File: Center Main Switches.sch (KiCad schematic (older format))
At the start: 120 parts

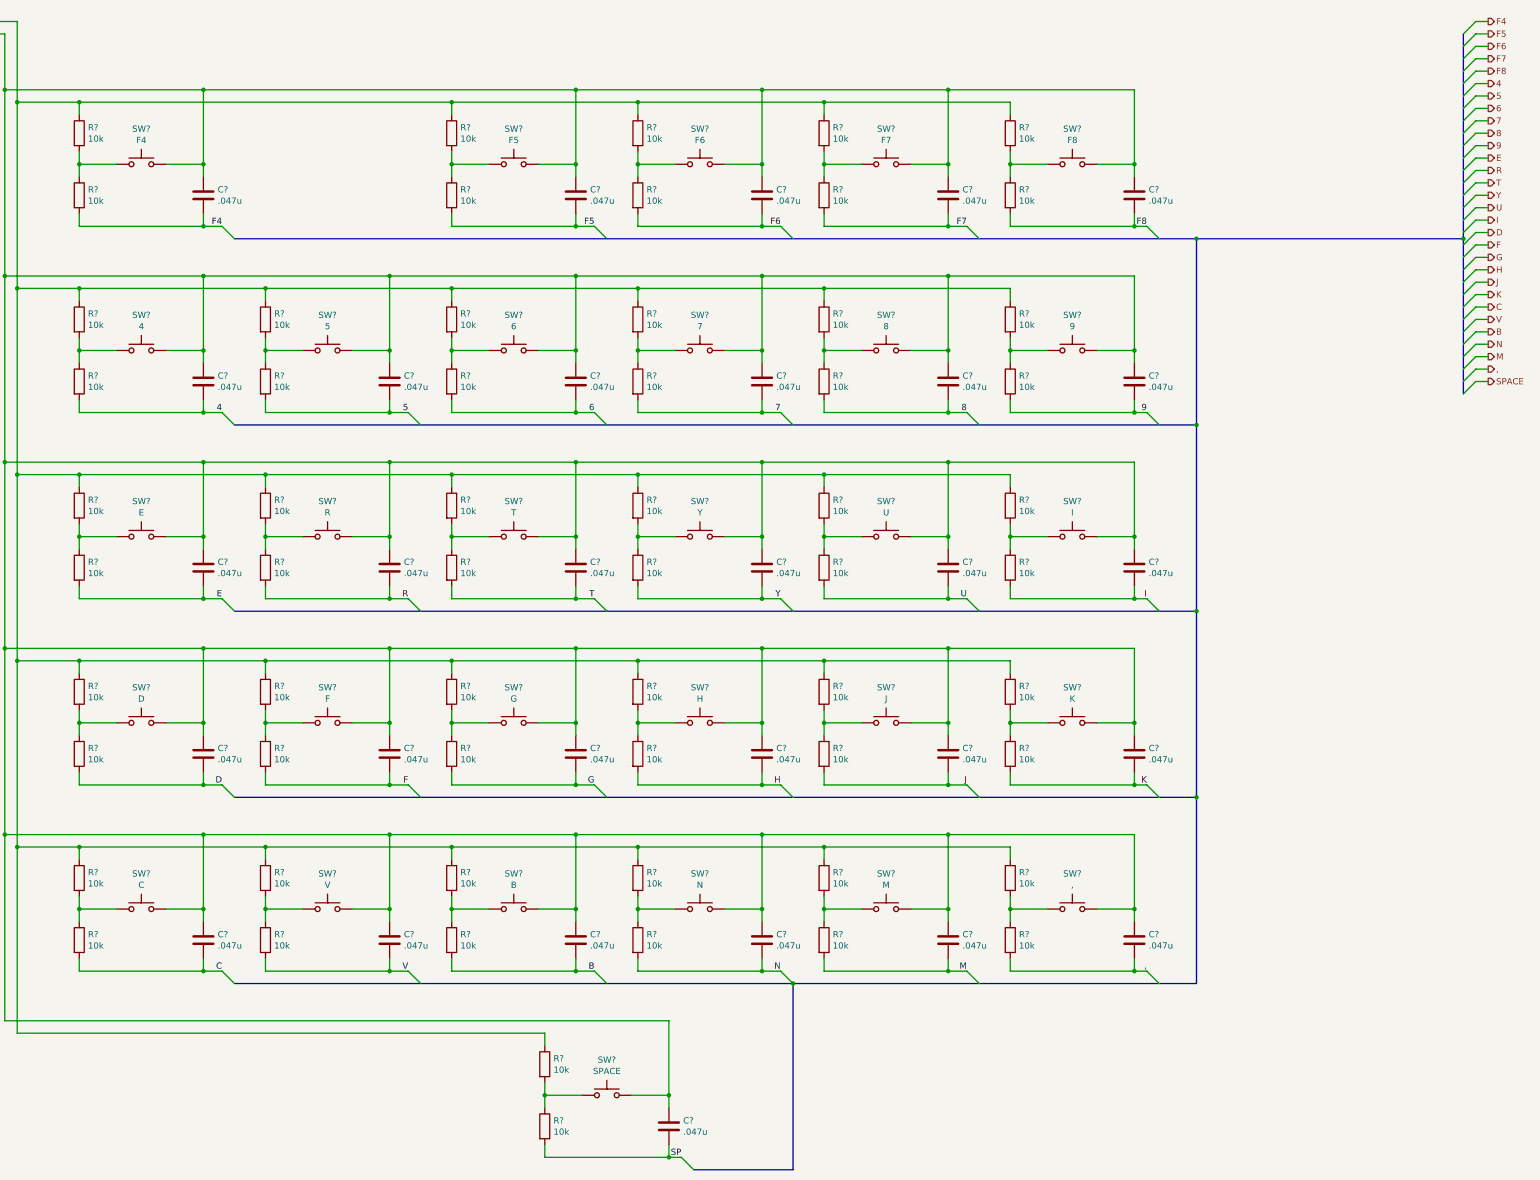
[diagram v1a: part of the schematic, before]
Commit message: Corrected errors found in design rule check
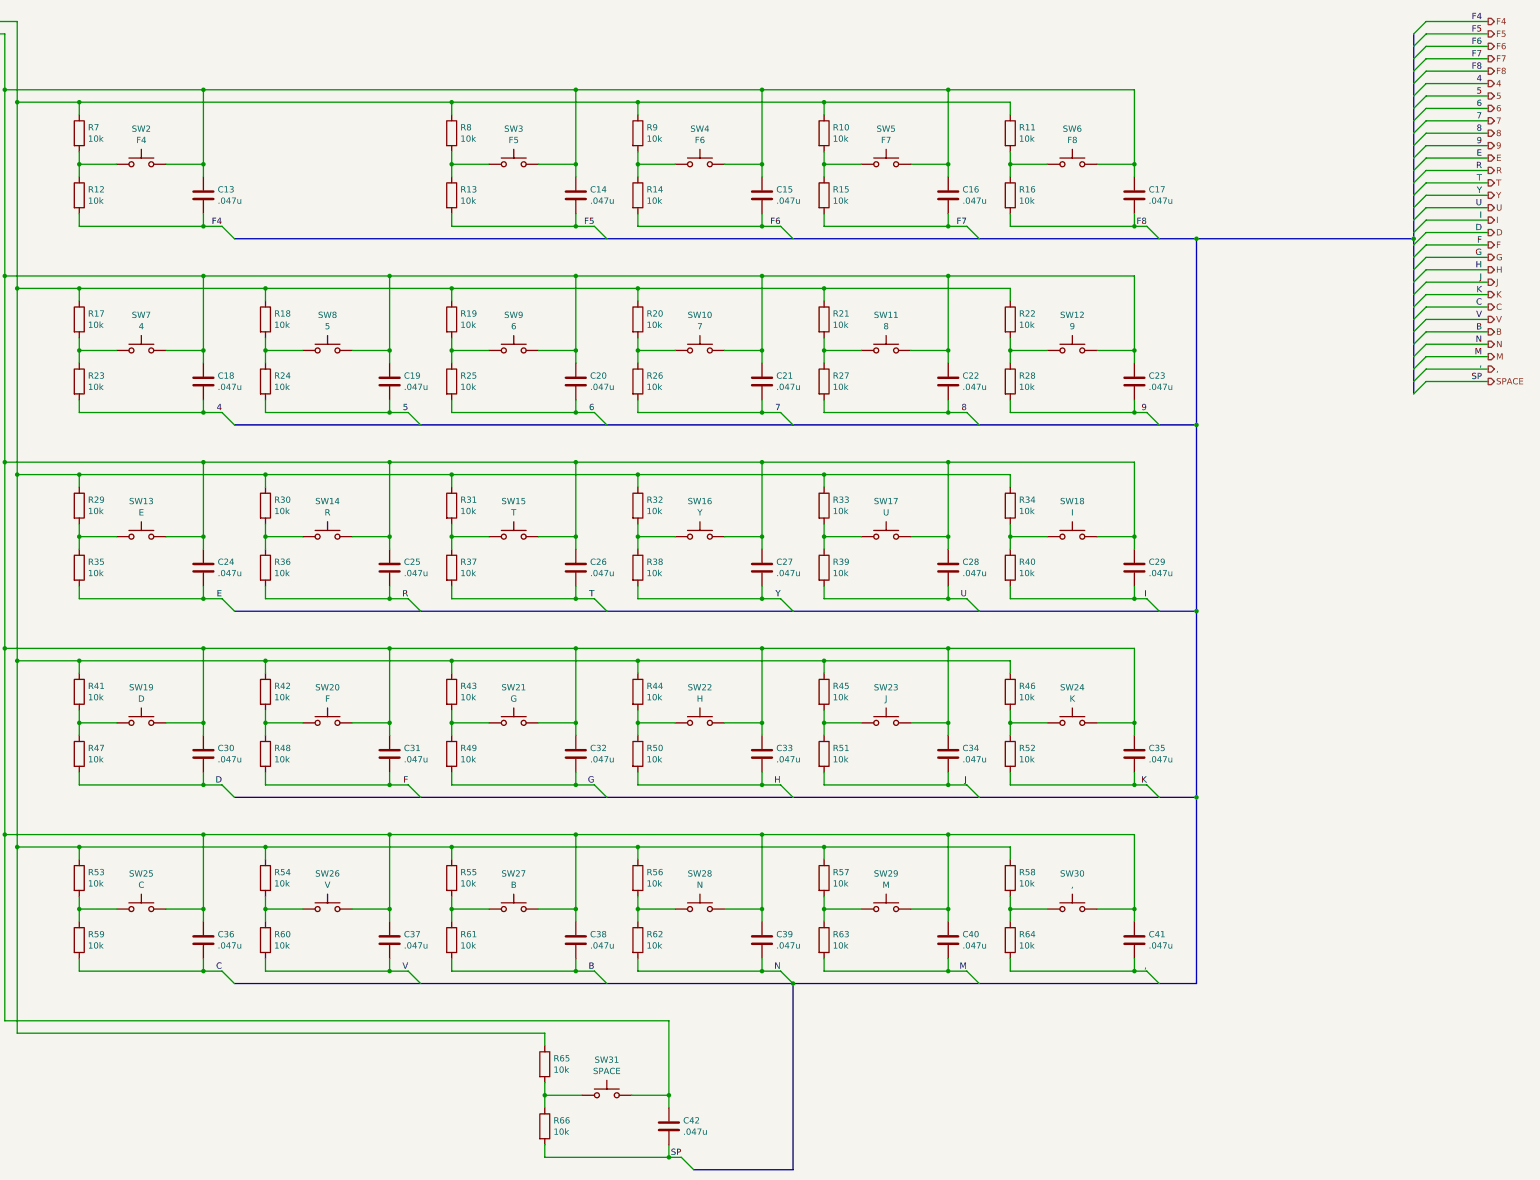
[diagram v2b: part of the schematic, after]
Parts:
- C13, C14, C15, C16, C17, C18, C19, C20, C21, C22, C23, C24, C25, C26, C27, C28, C29, C30, C31, C32, C33, C34, C35, C36, C37, C38, C39, C40, C41, C42: renamed from C?; footprint (none) -> Capacitor_SMD:C_1206_3216Metric_Pad1.42x1.75mm_HandSolder
- R10, R11, R12, R13, R14, R15, R16, R17, R18, R19, R20, R21, R22, R23, R24, R25, R26, R27, R28, R29, R30, R31, R32, R33, R34, R35, R36, R37, R38, R39, R40, R41, R42, R43, R44, R45, R46, R47, R48, R49, R50, R51, R52, R53, R54, R55, R56, R57, R58, R59, R60, R61, R62, R63, R64, R65, R66, R7, R8, R9: renamed from R?; footprint (none) -> Resistor_SMD:R_1206_3216Metric_Pad1.42x1.75mm_HandSolder
- SW10, SW11, SW12, SW13, SW14, SW15, SW16, SW17, SW18, SW19, SW2, SW20, SW21, SW22, SW23, SW24, SW25, SW26, SW27, SW28, SW29, SW3, SW30, SW31, SW4, SW5, SW6, SW7, SW8, SW9: renamed from SW?; footprint (none) -> Button_Switch_Keyboard:SW_Cherry_MX_1.00u_PCB
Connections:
- net SP is gone; now on net SPACE: C42.2, R66.2

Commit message: Redesigned for single large PCB
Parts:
- renumbered C13 to C24, C14 to C25, C15 to C26, C16 to C27, C17 to C28, C18 to C29, C19 to C30, C20 to C31, C21 to C32, C22 to C33, C23 to C34, C24 to C35, C25 to C36, C26 to C37, C27 to C38, C28 to C39, C29 to C40, C30 to C41, C31 to C42, C32 to C43, C33 to C44, C34 to C45, C35 to C46, C36 to C47, C37 to C48, C38 to C49, C39 to C50, C40 to C51, C41 to C52, C42 to C53
